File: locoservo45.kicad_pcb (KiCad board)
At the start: 2 copper layers, 95.2 x 42.5 mm, 21 parts, among them J1 RJ45, J10 Srv3_1, J11 Srv4_2, J12 Srv4_1, J13 Var1, J14 Var2, J15 Var3, J16 Var4, J2 RJ45, J3 RJ45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

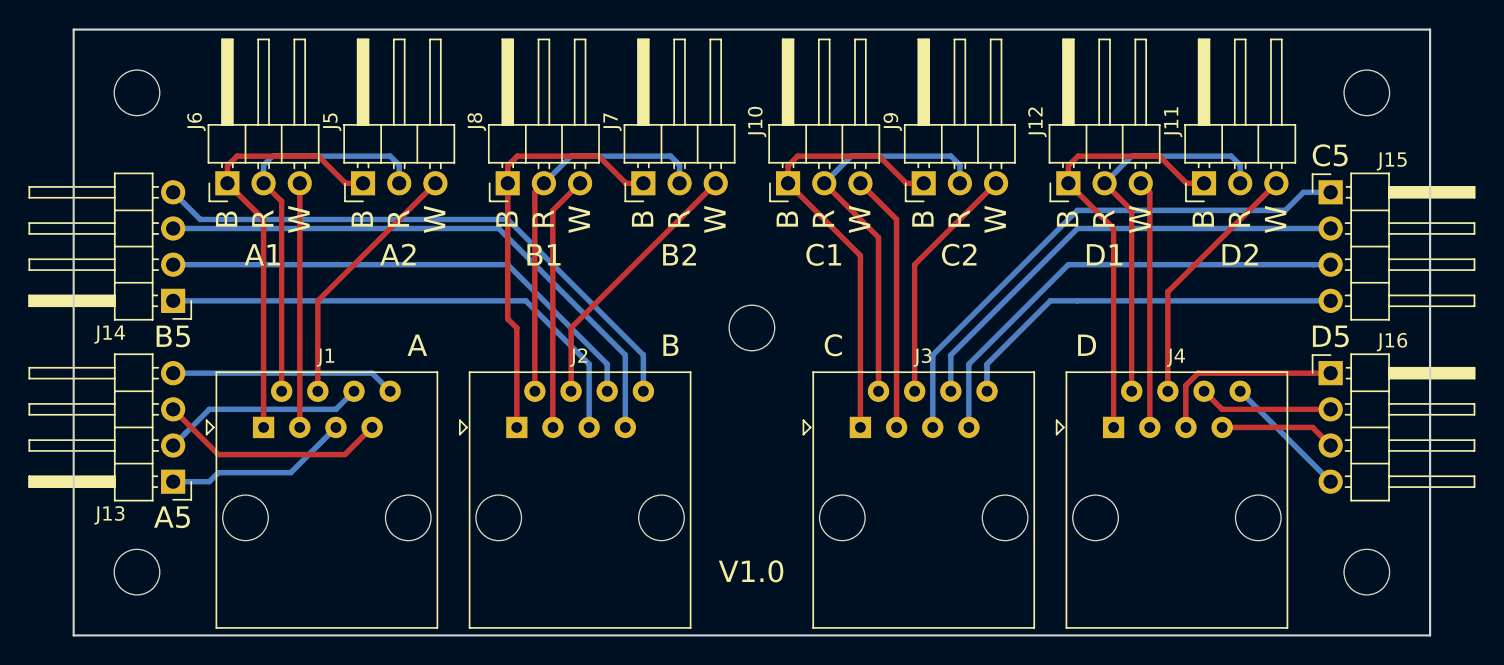
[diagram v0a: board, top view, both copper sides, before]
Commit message: added ground planes, re-routed connections
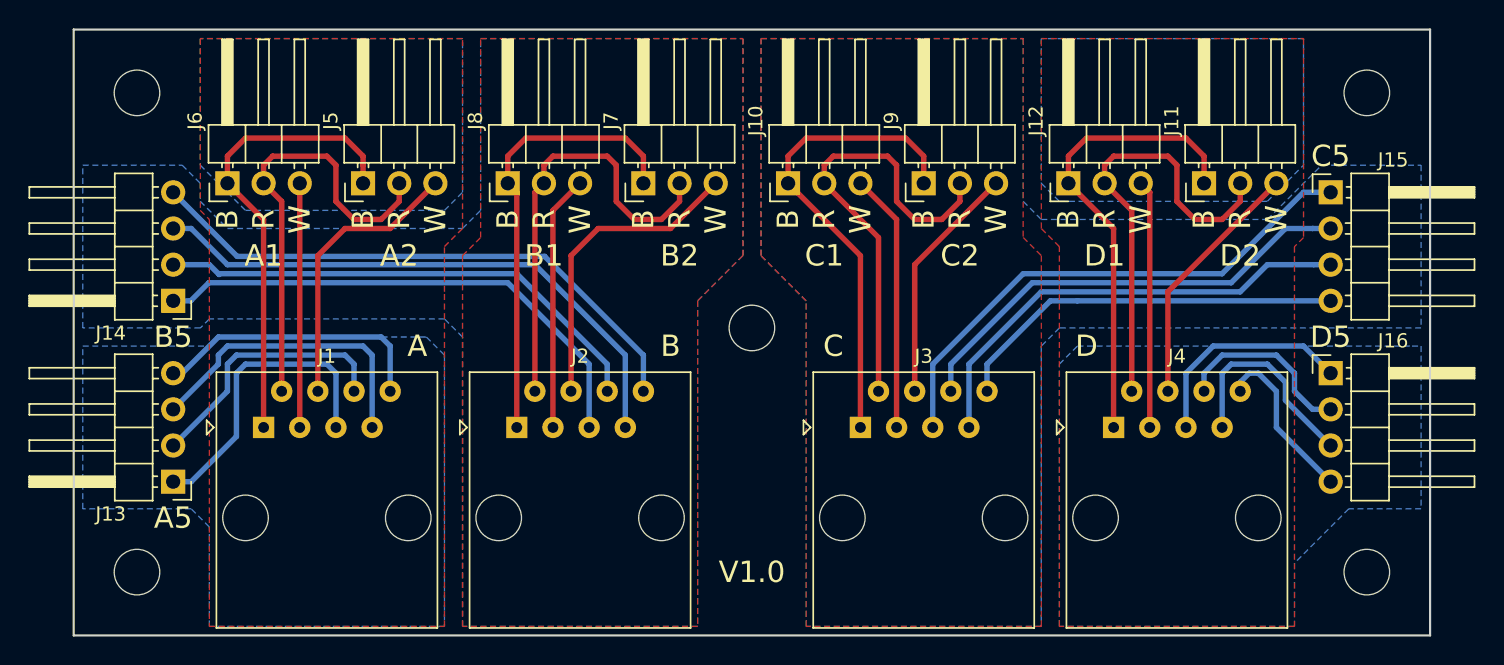
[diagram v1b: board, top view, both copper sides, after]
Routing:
- net Net-(J1-Pad5): track 13.0 -> 21.5 mm
- net Net-(J16-Pad3): track 8.15 -> 14.8 mm
- net Net-(J1-Pad7): track 16.1 -> 21.5 mm
- net Net-(J11-Pad2): track 27.2 -> 31.6 mm
- net Net-(J10-Pad2): track 28.0 -> 32.4 mm
- net Net-(J2-Pad2): track 26.7 -> 31.1 mm
- net Net-(J1-Pad6): track 14.3 -> 18.6 mm
- net Net-(J1-Pad8): track 15.8 -> 19.7 mm
- net Net-(J16-Pad2): track 9.42 -> 13.0 mm
- net Net-(J1-Pad2): track 27.7 -> 31.3 mm
- net Net-(J2-Pad4): track 18.8 -> 21.8 mm
- net Net-(J16-Pad4): track 8.98 -> 11.9 mm
- net Net-(J11-Pad1): track 30.3 -> 32.8 mm
- net Net-(J10-Pad1): track 31.1 -> 33.6 mm
- net Net-(J2-Pad1): track 29.2 -> 31.8 mm
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- added copper zone on B.Cu, net Net-(J1-Pad1)
- added copper zone on F.Cu, net Net-(J1-Pad1)
- added copper zone on B.Cu, net Net-(J10-Pad1)
- added copper zone on F.Cu, net Net-(J10-Pad1)
- added copper zone on B.Cu, net Net-(J11-Pad1)
- added copper zone on F.Cu, net Net-(J11-Pad1)
- added copper zone on B.Cu, net Net-(J2-Pad1)
- added copper zone on F.Cu, net Net-(J2-Pad1)

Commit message: v1.1
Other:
- board text added: "loco45 v1.1"
- board text removed: "V1.0"
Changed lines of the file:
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@@
-(kicad_pcb (version 20171130) (host pcbnew "(5.0.2)-1")
+(kicad_pcb (version 20171130) (host pcbnew 5.0.2+dfsg1-1)
   (general
     (thickness 1.6)
@@
   )
   (setup
-    (last_trace_width 0.381)
+    (last_trace_width 0.25)
     (user_trace_width 0.1524)
     (user_trace_width 0.254)
@@
   (gr_line (start 187.325 90.17) (end 187.325 132.715) (layer Edge.Cuts) (width 0.15))
   (gr_line (start 92.075 90.17) (end 187.325 90.17) (layer Edge.Cuts) (width 0.15))
-  (gr_text V1.0 (at 139.7 128.27) (layer F.SilkS)
+  (gr_text "loco45 v1.1" (at 139.7 124.55 90) (layer F.SilkS)
     (effects (font (size 1.5 1.5) (thickness 0.3)))
   )
